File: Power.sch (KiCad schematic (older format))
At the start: 30 parts, among them IC3 IRSM005, IC4 IRSM005, IC5 IRSM005, U2 ACS730xLCTR-50AB, U3 ACS730xLCTR-50AB, U4 ACS730xLCTR-50AB

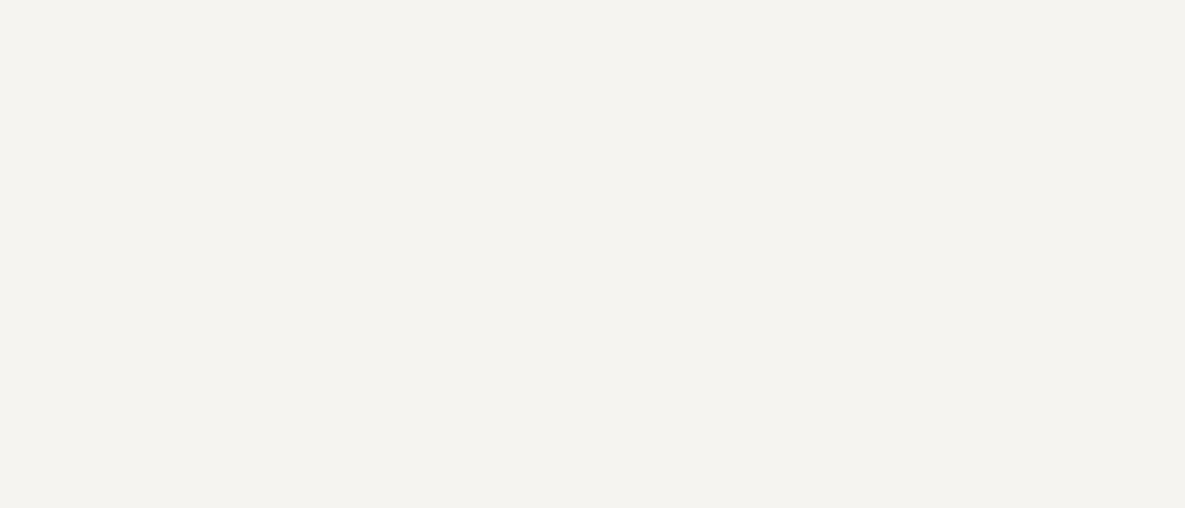
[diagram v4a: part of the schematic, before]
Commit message: - replaced L2 by 0805 coil - added a load of DC link caps - finalized layout
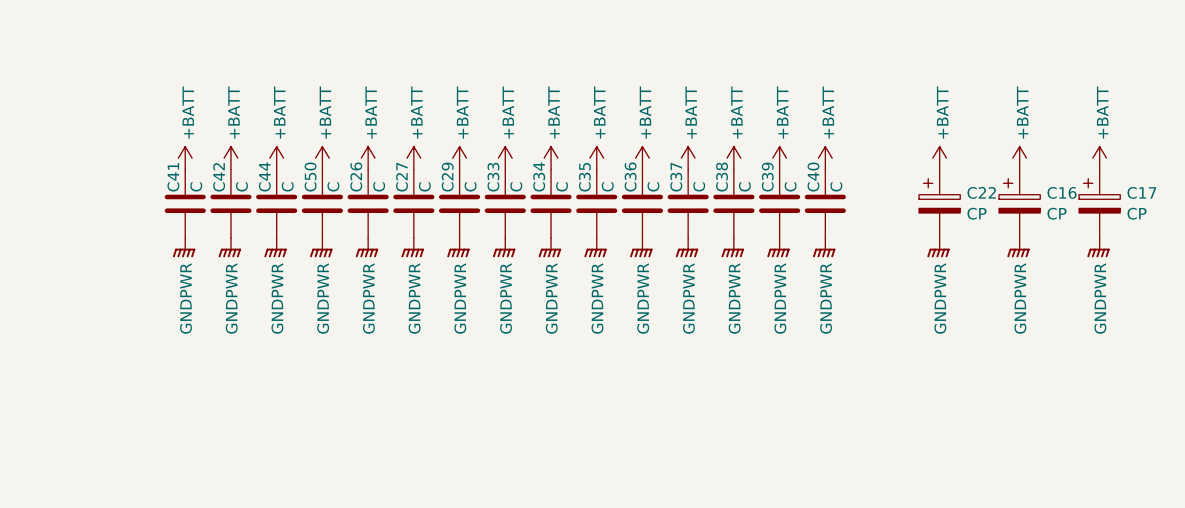
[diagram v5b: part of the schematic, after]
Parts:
- added C16, C17, C22: CP, Capacitor_THT:CP_Radial_D6.3mm_P2.50mm, symbol Device:CP
- added C26, C27, C29, C33, C34, C35, C36, C37, C38, C39, C40, C41, C42, C44, C50: C, Capacitor_SMD:C_1206_3216Metric, symbol Device:C
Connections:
- net +BATT: now also C16.1, C17.1, C22.1, C26.1, C27.1, C29.1, C33.1, C34.1, C35.1, C36.1, C37.1, C38.1, C39.1, C40.1, C41.1, C42.1, C44.1, C50.1
- net GNDPWR: now also C16.2, C17.2, C22.2, C26.2, C27.2, C29.2, C33.2, C34.2, C35.2, C36.2, C37.2, C38.2, C39.2, C40.2, C41.2, C42.2, C44.2, C50.2

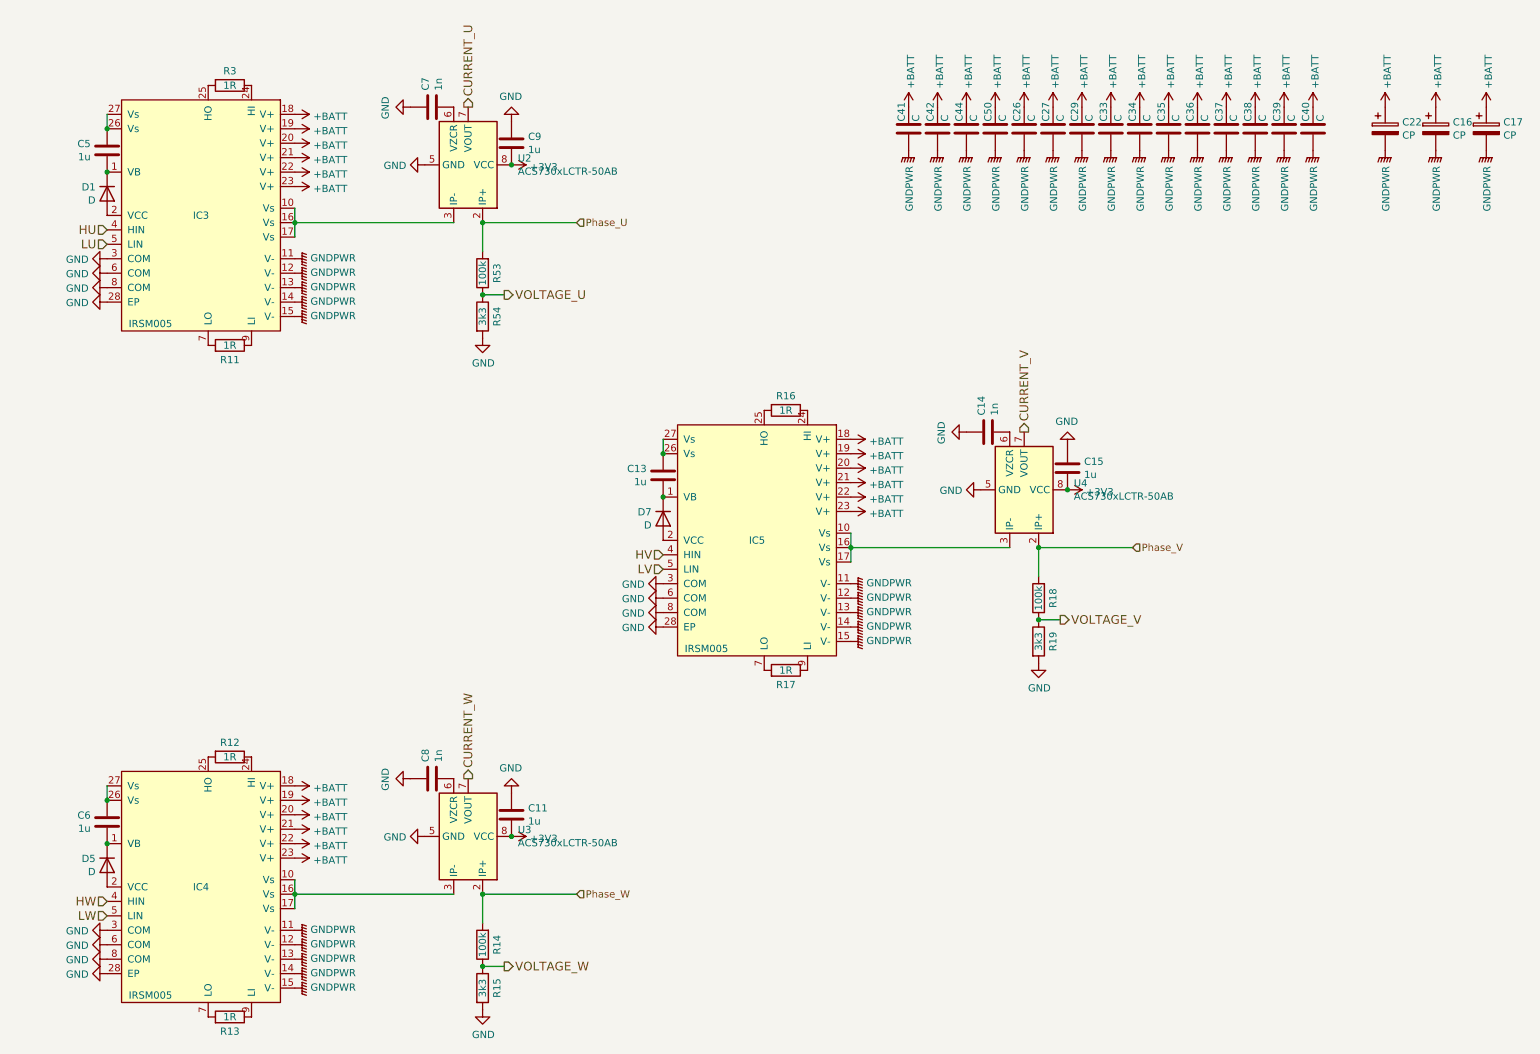
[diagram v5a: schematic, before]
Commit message: - connected VCC of gatedrivers to VCC (doh)
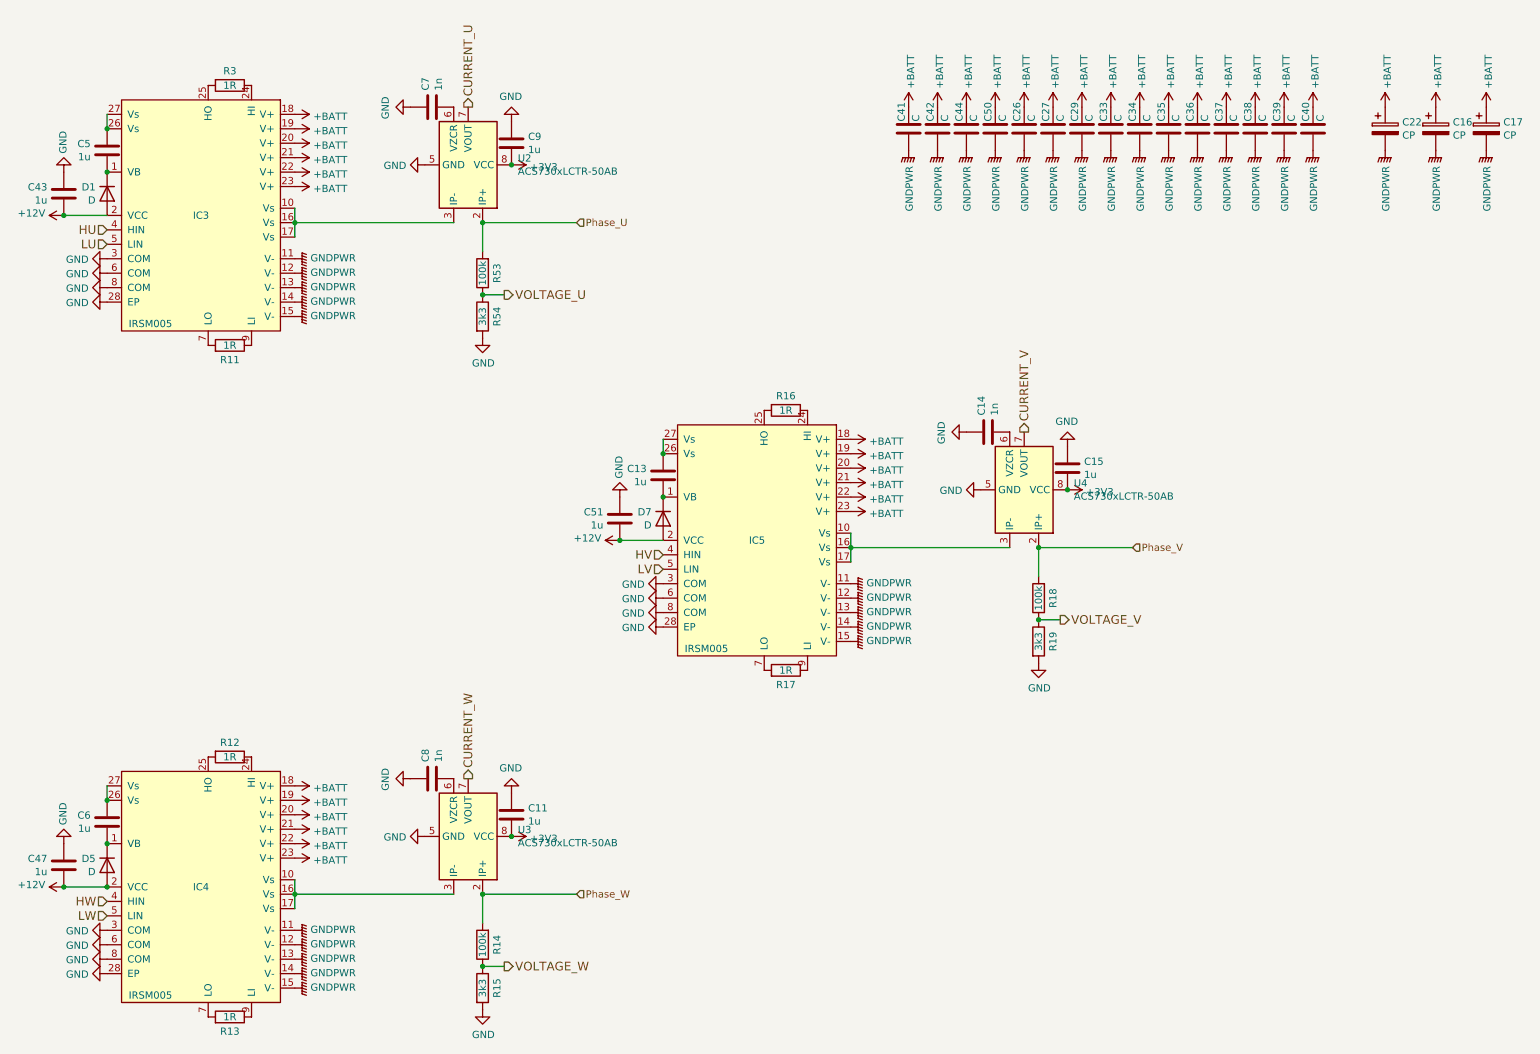
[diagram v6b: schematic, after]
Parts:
- added C43, C47, C51: 1u, Capacitor_SMD:C_0805_2012Metric, symbol Device:C
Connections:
- net GND: now also C43.2, C47.2, C51.2
- net +12V: now reaches D1.2 (A), IC3.2 (VCC)
- net +12V: now also D5.2 (A), D7.2 (A), IC4.2 (VCC), IC5.2 (VCC), C43.1, C47.1, C51.1
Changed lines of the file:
@@
 	1    0    0    -1
 $EndComp
+$Comp
+L power:+12V #PWR0228
+U 1 1 5F331310
+P 900 6550
+F 0 "#PWR0228" H 900 6400 50  0001 C CNN
+F 1 "+12V" V 915 6678 50  0000 L CNN
+F 2 "" H 900 6550 50  0001 C CNN
+F 3 "" H 900 6550 50  0001 C CNN
+	1    900  6550
+	0    -1   -1   0
+$EndComp
+$Comp
+L Device:C C47
+U 1 1 5F332710
+P 900 6400
+F 0 "C47" H 786 6354 50  0000 R CNN
+F 1 "1u" H 786 6445 50  0000 R CNN
+F 2 "Capacitor_SMD:C_0805_2012Metric" H 938 6250 50  0001 C CNN
+F 3 "~" H 900 6400 50  0001 C CNN
+	1    900  6400
+	1    0    0    1
+$EndComp
+Wire Wire Line
+	900  6550 1200 6550
+Connection ~ 900  6550
+Connection ~ 1200 6550
+$Comp
+L power:GND #PWR0229
+U 1 1 5F333A5F
+P 900 6250
+F 0 "#PWR0229" H 900 6000 50  0001 C CNN
+F 1 "GND" V 905 6122 50  0000 R CNN
+F 2 "" H 900 6250 50  0001 C CNN
+F 3 "" H 900 6250 50  0001 C CNN
+	1    900  6250
+	-1   0    0    1
+$EndComp
+$Comp
+L power:+12V #PWR0230
+U 1 1 5F336CC1
+P 4750 4150
+F 0 "#PWR0230" H 4750 4000 50  0001 C CNN
+F 1 "+12V" V 4765 4278 50  0000 L CNN
+F 2 "" H 4750 4150 50  0001 C CNN
+F 3 "" H 4750 4150 50  0001 C CNN
+	1    4750 4150
+	0    -1   -1   0
+$EndComp
+$Comp
+L Device:C C51
+U 1 1 5F336CC7
+P 4750 4000
+F 0 "C51" H 4636 3954 50  0000 R CNN
+F 1 "1u" H 4636 4045 50  0000 R CNN
+F 2 "Capacitor_SMD:C_0805_2012Metric" H 4788 3850 50  0001 C CNN
+F 3 "~" H 4750 4000 50  0001 C CNN
+	1    4750 4000
+	1    0    0    1
+$EndComp
+Wire Wire Line
+	4750 4150 5050 4150
+Connection ~ 4750 4150
+$Comp
+L power:GND #PWR0231
+U 1 1 5F336CCF
+P 4750 3850
+F 0 "#PWR0231" H 4750 3600 50  0001 C CNN
+F 1 "GND" V 4755 3722 50  0000 R CNN
+F 2 "" H 4750 3850 50  0001 C CNN
+F 3 "" H 4750 3850 50  0001 C CNN
+	1    4750 3850
+	-1   0    0    1
+$EndComp
+$Comp
+L power:+12V #PWR0232
+U 1 1 5F3378E0
+P 900 1900
+F 0 "#PWR0232" H 900 1750 50  0001 C CNN
+F 1 "+12V" V 915 2028 50  0000 L CNN
+F 2 "" H 900 1900 50  0001 C CNN
+F 3 "" H 900 1900 50  0001 C CNN
+	1    900  1900
+	0    -1   -1   0
+$EndComp
+$Comp
+L Device:C C43
+U 1 1 5F3378E6
+P 900 1750
+F 0 "C43" H 786 1704 50  0000 R CNN
+F 1 "1u" H 786 1795 50  0000 R CNN
+F 2 "Capacitor_SMD:C_0805_2012Metric" H 938 1600 50  0001 C CNN
+F 3 "~" H 900 1750 50  0001 C CNN
+	1    900  1750
+	1    0    0    1
+$EndComp
+Wire Wire Line
+	900  1900 1200 1900
+Connection ~ 900  1900
+$Comp
+L power:GND #PWR0233
+U 1 1 5F3378EE
+P 900 1600
+F 0 "#PWR0233" H 900 1350 50  0001 C CNN
+F 1 "GND" V 905 1472 50  0000 R CNN
+F 2 "" H 900 1600 50  0001 C CNN
+F 3 "" H 900 1600 50  0001 C CNN
+	1    900  1600
+	-1   0    0    1
+$EndComp
 $EndSCHEMATC

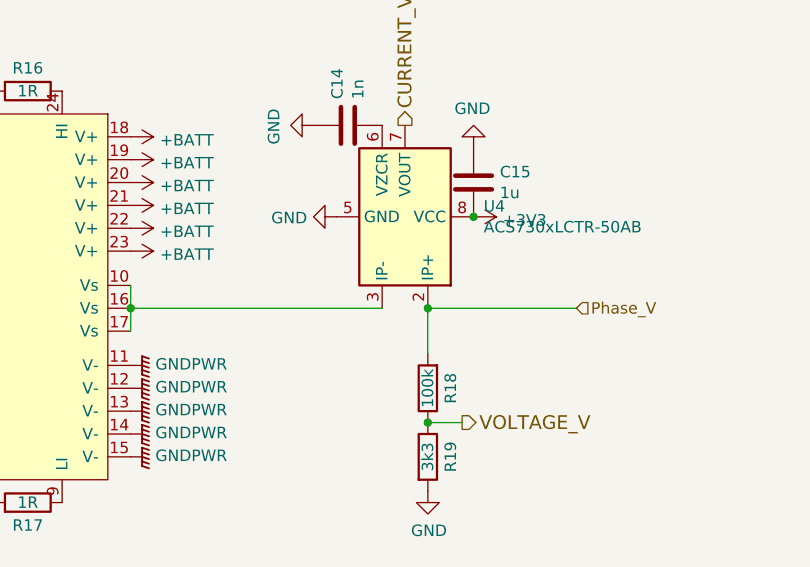
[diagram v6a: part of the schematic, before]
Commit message: - added jumper under hall for assembly option
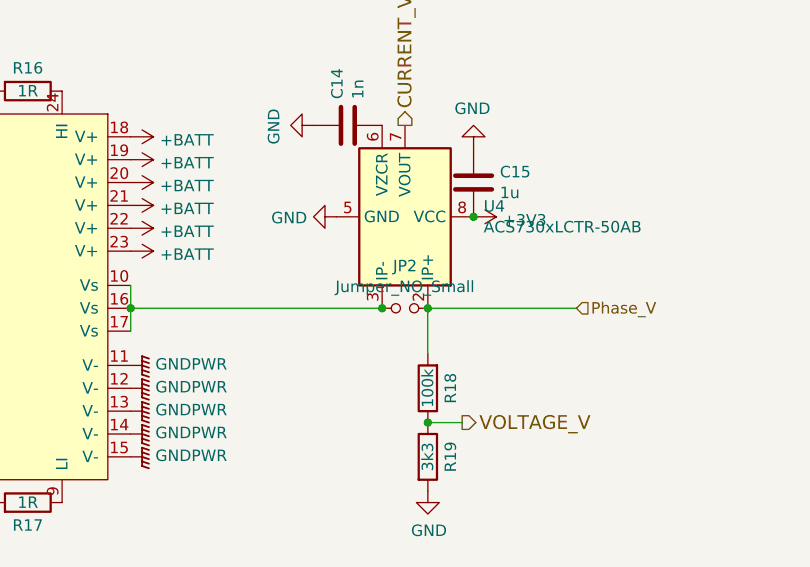
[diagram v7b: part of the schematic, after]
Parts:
- added JP2: Jumper_NO_Small, Jumper:SolderJumper-2_P1.3mm_Open_RoundedPad1.0x1.5mm, symbol Device:Jumper_NO_Small
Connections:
- net Phase_V: now also JP2.2
- net at IC5.10 (Vs), IC5.16 (Vs), IC5.17 (Vs)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: now also JP2.1
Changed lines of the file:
@@
 	-1   0    0    1
 $EndComp
+$Comp
+L Device:Jumper_NO_Small JP2
+U 1 1 5F5CEC3F
+P 7550 4200
+F 0 "JP2" H 7550 4385 50  0000 C CNN
+F 1 "Jumper_NO_Small" H 7550 4294 50  0000 C CNN
+F 2 "Jumper:SolderJumper-2_P1.3mm_Open_RoundedPad1.0x1.5mm" H 7550 4200 50  0001 C CNN
+F 3 "~" H 7550 4200 50  0001 C CNN
+	1    7550 4200
+	1    0    0    -1
+$EndComp
+Connection ~ 7450 4200
 $EndSCHEMATC

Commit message: - changed current sensors - updated symbols - exported for production
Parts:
- removed C14, C7, C8: 1n, Capacitor_SMD:C_0805_2012Metric, symbol Device:C
- C16, C17, C22: symbol Device:CP -> Device:C_Polarized
- JP2: value Jumper_NO_Small -> 2SHUNT; footprint Jumper:SolderJumper-2_P1.3mm_Open_RoundedPad1.0x1.5mm -> Jumper:SolderJumper-2_P1.3mm_Open_TrianglePad1.0x1.5mm; symbol Device:Jumper_NO_Small -> Jumper:SolderJumper_2_Open
- U2, U3, U4: symbol Revolterlib:ACS730xLCTR-50AB -> Sensor_Current:ACS722xLCTR-40AB
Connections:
- net GND: now also U2.6 (BW_SEL), U3.6 (BW_SEL), U4.6 (BW_SEL)
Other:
- moved on the sheet: C11, C15, C9, R14, R15, R18, R19, R53, R54
